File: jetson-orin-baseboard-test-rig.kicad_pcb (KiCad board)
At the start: 2 copper layers, 150 x 150 mm, 153 parts, among them J1 PinHeader_2x6_P2.54mm_Drill1.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, J2 PinHeader_2x6_P2.54mm_Drill1.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, J3 PinHeader_2x6_P2.54mm_Drill1.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, J4 PinHeader_2x6_P2.54mm_Drill1.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, J5 PinHeader_2x6_P2.54mm_Drill1.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, J6 PinHeader_2x6_P2.54mm_Drill1.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, J7 PinHeader_2x6_P2.54mm_Drill1.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, J9 Tag-Connect_TC2050-IDC-NL_2x5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

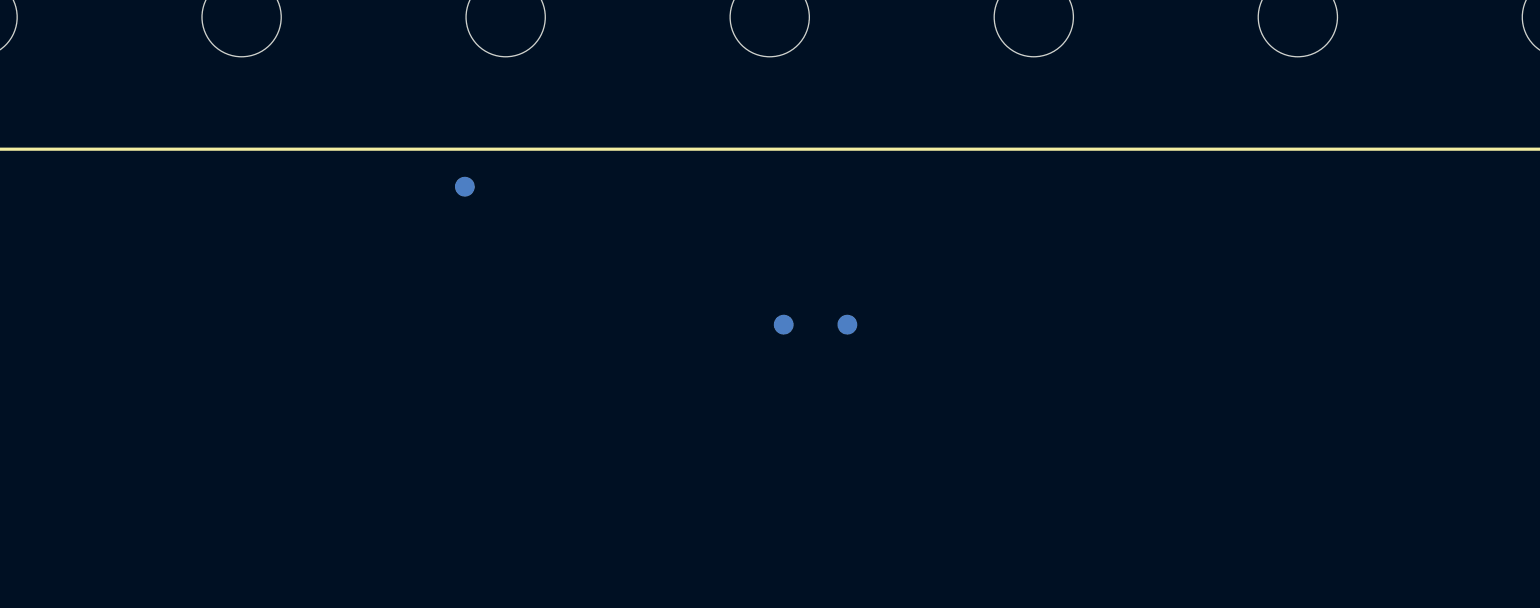
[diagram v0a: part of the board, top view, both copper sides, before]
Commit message: [#77400] Add spring probes (WiP)
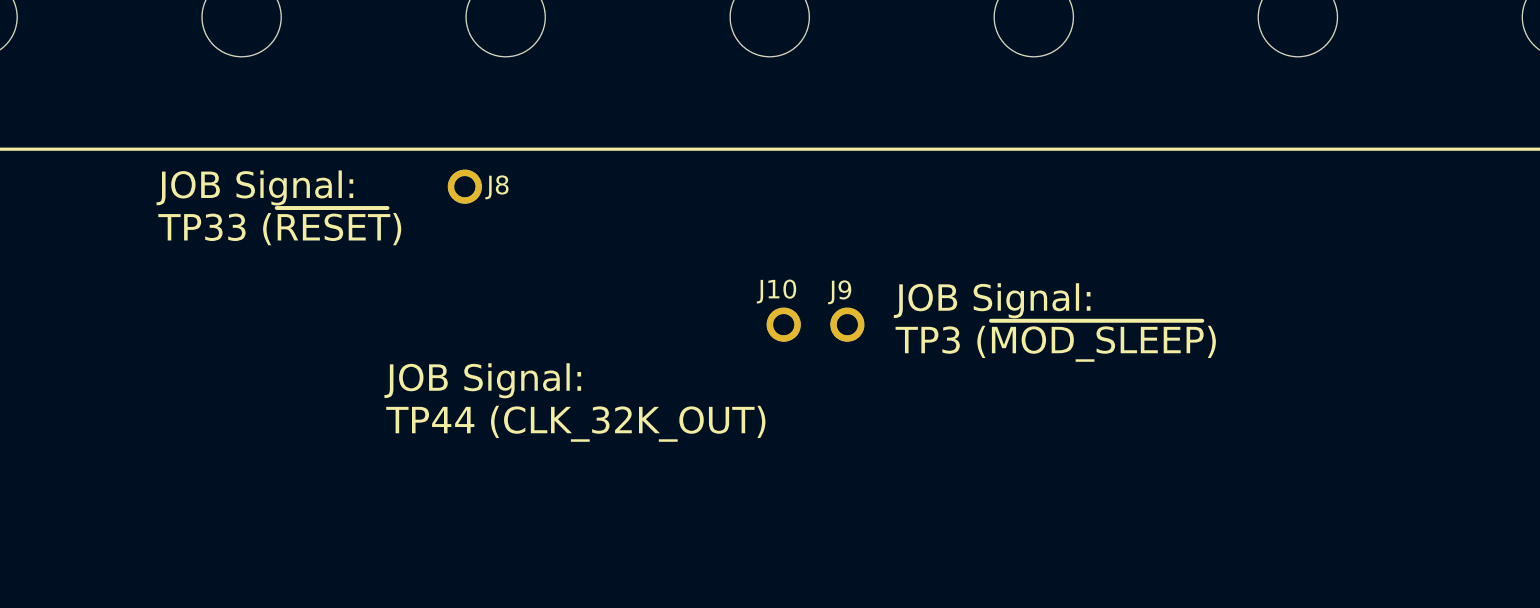
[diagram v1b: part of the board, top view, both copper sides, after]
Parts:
- removed TP3, TP33, TP44: TP_0.75mm_SMD, antmicro-footprints:TP_SMD_0.75mm
- added J10: Harwin_1x1_H17.75mm_Drill0.8mm_S13-503, antmicro-footprints:PogoPin_Harwin_1x1_H17.75mm_Drill0.8mm_S13-503, F.Cu at (210.5, 101.6)
- added J8: Harwin_1x1_H17.75mm_Drill0.8mm_S13-503, antmicro-footprints:PogoPin_Harwin_1x1_H17.75mm_Drill0.8mm_S13-503, F.Cu at (198.5, 96.4)
- added J9: Harwin_1x1_H17.75mm_Drill0.8mm_S13-503, antmicro-footprints:PogoPin_Harwin_1x1_H17.75mm_Drill0.8mm_S13-503, F.Cu at (212.9, 101.6)
- renumbered J9 to J999
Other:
- board text added: "JOB Signal: TP3 (~{MOD_SLEEP})"
- board text added: "JOB Signal: TP33 (~{RESET})"
- board text added: "JOB Signal: TP44 (CLK_32K_OUT)"

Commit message: [#77400] Finalize schematic
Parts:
- removed J999: Tag-Connect_TC2050-IDC-NL_2x5_P1.27mm, antmicro-footprints:Tag-Connect_TC2050-IDC-NL_2x5_P1.27mm
- removed TP1, TP13, TP14, TP17, TP22, TP23, TP29, TP30, TP31, TP32, TP52, TP53, TP54, TP55: TP_0.75mm_SMD, antmicro-footprints:TP_SMD_0.75mm
- added D1: LED_G_0603_KP-1608CGCK, antmicro-footprints:LED_0603_1608Metric_G, F.Cu at (298.6, 192.4)
- added D2: LED_G_0603_KP-1608CGCK, antmicro-footprints:LED_0603_1608Metric_G, F.Cu at (296.0, 192.4)
- added J11: Harwin_1x1_H17.75mm_Drill0.8mm_S13-503, antmicro-footprints:PogoPin_Harwin_1x1_H17.75mm_Drill0.8mm_S13-503, F.Cu at (199.0, 123.2)
- added J12: Harwin_1x1_H17.75mm_Drill0.8mm_S13-503, antmicro-footprints:PogoPin_Harwin_1x1_H17.75mm_Drill0.8mm_S13-503, F.Cu at (221.8, 128.6)
- added J13: Harwin_1x1_H17.75mm_Drill0.8mm_S13-503, antmicro-footprints:PogoPin_Harwin_1x1_H17.75mm_Drill0.8mm_S13-503, F.Cu at (243.3, 141.7)
- added J14: Harwin_1x1_H17.75mm_Drill0.8mm_S13-503, antmicro-footprints:PogoPin_Harwin_1x1_H17.75mm_Drill0.8mm_S13-503, F.Cu at (247.2, 130.3)
- added J15: Harwin_1x1_H17.75mm_Drill0.8mm_S13-503, antmicro-footprints:PogoPin_Harwin_1x1_H17.75mm_Drill0.8mm_S13-503, F.Cu at (214.9, 141.1)
- added J16: Harwin_1x1_H17.75mm_Drill0.8mm_S13-503, antmicro-footprints:PogoPin_Harwin_1x1_H17.75mm_Drill0.8mm_S13-503, F.Cu at (203.4, 141.8)
- added J17: Harwin_1x1_H17.75mm_Drill0.8mm_S13-503, antmicro-footprints:PogoPin_Harwin_1x1_H17.75mm_Drill0.8mm_S13-503, F.Cu at (203.4, 143.3)
- added J18: Harwin_1x1_H17.75mm_Drill0.8mm_S13-503, antmicro-footprints:PogoPin_Harwin_1x1_H17.75mm_Drill0.8mm_S13-503, F.Cu at (203.4, 144.8)
- added J19: Harwin_1x1_H17.75mm_Drill0.8mm_S13-503, antmicro-footprints:PogoPin_Harwin_1x1_H17.75mm_Drill0.8mm_S13-503, F.Cu at (203.4, 146.3)
- added J20: Harwin_1x1_H17.75mm_Drill0.8mm_S13-503, antmicro-footprints:PogoPin_Harwin_1x1_H17.75mm_Drill0.8mm_S13-503, F.Cu at (203.4, 147.8)
- added J21: Harwin_1x1_H17.75mm_Drill0.8mm_S13-503, antmicro-footprints:PogoPin_Harwin_1x1_H17.75mm_Drill0.8mm_S13-503, F.Cu at (203.4, 149.3)
- added J22: Harwin_1x1_H17.75mm_Drill0.8mm_S13-503, antmicro-footprints:PogoPin_Harwin_1x1_H17.75mm_Drill0.8mm_S13-503, F.Cu at (203.4, 150.8)
- added J23: Harwin_1x1_H17.75mm_Drill0.8mm_S13-503, antmicro-footprints:PogoPin_Harwin_1x1_H17.75mm_Drill0.8mm_S13-503, F.Cu at (203.4, 152.3)
- added J24: Harwin_1x1_H17.75mm_Drill0.8mm_S13-503, antmicro-footprints:PogoPin_Harwin_1x1_H17.75mm_Drill0.8mm_S13-503, F.Cu at (203.4, 153.8)
- added J25: Harwin_1x1_H17.75mm_Drill0.8mm_S13-503, antmicro-footprints:PogoPin_Harwin_1x1_H17.75mm_Drill0.8mm_S13-503, F.Cu at (221.8, 152.0)
- added J26: Harwin_1x1_H17.75mm_Drill0.8mm_S13-503, antmicro-footprints:PogoPin_Harwin_1x1_H17.75mm_Drill0.8mm_S13-503, F.Cu at (220.3, 152.2)
- added J27: Harwin_1x1_H17.75mm_Drill0.8mm_S13-503, antmicro-footprints:PogoPin_Harwin_1x1_H17.75mm_Drill0.8mm_S13-503, F.Cu at (217.9, 152.1)
- added J28: Harwin_1x1_H17.75mm_Drill0.8mm_S13-503, antmicro-footprints:PogoPin_Harwin_1x1_H17.75mm_Drill0.8mm_S13-503, F.Cu at (216.6, 150.9)
- added J29: Harwin_1x1_H17.75mm_Drill0.8mm_S13-503, antmicro-footprints:PogoPin_Harwin_1x1_H17.75mm_Drill0.8mm_S13-503, F.Cu at (219.2, 150.9)
- added J30: Harwin_1x1_H17.75mm_Drill0.8mm_S13-503, antmicro-footprints:PogoPin_Harwin_1x1_H17.75mm_Drill0.8mm_S13-503, F.Cu at (216.8, 120.1)
- added Q1: BSS84, antmicro-footprints:SOT-23-3, F.Cu at (246.2, 111.7)
- added R1: R_330R_0402, antmicro-footprints:R_0402_1005Metric, F.Cu at (298.6, 190.0)
- added R10: R_0R_0402, antmicro-footprints:R_0402_1005Metric, F.Cu at (239.6, 112.5)
- added R11: R_0R_0402, antmicro-footprints:R_0402_1005Metric, F.Cu at (239.6, 114.5)
- added R12: R_0R_0402, antmicro-footprints:R_0402_1005Metric, F.Cu at (239.6, 116.5)
- added R13: R_3k9_0402, antmicro-footprints:R_0402_1005Metric, F.Cu at (239.6, 118.5)
- added R14: R_68k_0402, antmicro-footprints:R_0402_1005Metric, F.Cu at (239.6, 120.5)
- added R15: R_68k_0402, antmicro-footprints:R_0402_1005Metric, F.Cu at (242.5, 110.6)
- added R16: R_68k_0402, antmicro-footprints:R_0402_1005Metric, F.Cu at (242.5, 112.5)
- added R17: R_68k_0402, antmicro-footprints:R_0402_1005Metric, F.Cu at (242.5, 114.5)
- added R18: R_0R_0402, antmicro-footprints:R_0402_1005Metric, F.Cu at (242.5, 116.5)
- added R19: R_10k_0402, antmicro-footprints:R_0402_1005Metric, F.Cu at (242.5, 118.5)
- added R2: R_3k9_0402, antmicro-footprints:R_0402_1005Metric, F.Cu at (296.0, 190.0)
- added R3: R_0R_0402, antmicro-footprints:R_0402_1005Metric, F.Cu at (236.7, 110.6)
- added R4: R_10k_0402, antmicro-footprints:R_0402_1005Metric, F.Cu at (236.7, 112.5)
- added R5: R_0R_0402, antmicro-footprints:R_0402_1005Metric, F.Cu at (236.7, 114.5)
- added R6: R_0R_0402, antmicro-footprints:R_0402_1005Metric, F.Cu at (236.7, 116.5)
- added R7: R_0R_0402, antmicro-footprints:R_0402_1005Metric, F.Cu at (236.7, 118.5)
- added R8: R_0R_0402, antmicro-footprints:R_0402_1005Metric, F.Cu at (236.7, 120.5)
- added R9: R_0R_0402, antmicro-footprints:R_0402_1005Metric, F.Cu at (239.6, 110.6)
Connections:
- J8 pad 1: /GPIO_00 -> Net-(J8-Pad1)
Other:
- board text added: "JOB Signal: SP7-Pin1 (GND)"
- board text added: "JOB Signal: TP13 (U6-Pin30)"
- board text added: "JOB Signal: TP17 (USBC0_VBUS)- TP1 (USBC3_VBUS)- TP29 (USBC1_VBUS)- TP14 (VCC)- TP53 (+5V)- TP54 (+3V3)- TP52 (3V3_STDB)- TP55 (+1V8)- TP23 (GND)-"
- board text added: "JOB Signal: TP22 (HDMI_HPD)"
- board text added: "JOB Signal: TP30 (USBC_HPD)"
- board text added: "JOB Signal: TP31 (USBC1_DIR)"
- board text added: "JOB Signal: TP32 (USBC1_FAULT_N)"
- board text removed: "+1V8"
- board text removed: "+3V3"
- board text removed: "+5V"
- board text removed: "3V3 STDB"
- board text removed: "EEPROM SPI"
- board text removed: "GND"
- board text removed: "VBUS0"
- board text removed: "VBUS1"
- board text removed: "VBUS3"
- board text removed: "VCC"

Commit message: [#77400] Finish routing
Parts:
- added REF**29: MP_NPTH_Drill3mm, antmicro-footprints:MP_NPTH_Drill3mm, F.Cu at (220.0, 110.0)
- added REF**29: MP_NPTH_Drill3mm, antmicro-footprints:MP_NPTH_Drill3mm, F.Cu at (170.0, 110.0)
- added REF**30: MP_NPTH_Drill3mm, antmicro-footprints:MP_NPTH_Drill3mm, F.Cu at (230.0, 110.0)
- added REF**30: MP_NPTH_Drill3mm, antmicro-footprints:MP_NPTH_Drill3mm, F.Cu at (180.0, 100.0)
- added REF**30: MP_NPTH_Drill3mm, antmicro-footprints:MP_NPTH_Drill3mm, F.Cu at (180.0, 110.0)
- added REF**31: MP_NPTH_Drill3mm, antmicro-footprints:MP_NPTH_Drill3mm, F.Cu at (190.0, 110.0)
- added REF**31: MP_NPTH_Drill3mm, antmicro-footprints:MP_NPTH_Drill3mm, F.Cu at (240.0, 110.0)
- added REF**32: MP_NPTH_Drill3mm, antmicro-footprints:MP_NPTH_Drill3mm, F.Cu at (170.0, 140.0)
- added REF**32: MP_NPTH_Drill3mm, antmicro-footprints:MP_NPTH_Drill3mm, F.Cu at (280.0, 120.0)
- added REF**32: MP_NPTH_Drill3mm, antmicro-footprints:MP_NPTH_Drill3mm, F.Cu at (190.0, 130.0)
- added REF**32: MP_NPTH_Drill3mm, antmicro-footprints:MP_NPTH_Drill3mm, F.Cu at (240.0, 120.0)
- added REF**32: MP_NPTH_Drill3mm, antmicro-footprints:MP_NPTH_Drill3mm, F.Cu at (190.0, 120.0)
- added REF**32: MP_NPTH_Drill3mm, antmicro-footprints:MP_NPTH_Drill3mm, F.Cu at (200.0, 130.0)
- added REF**32: MP_NPTH_Drill3mm, antmicro-footprints:MP_NPTH_Drill3mm, F.Cu at (250.0, 110.0)
- added REF**32: MP_NPTH_Drill3mm, antmicro-footprints:MP_NPTH_Drill3mm, F.Cu at (270.0, 110.0)
- added REF**32: MP_NPTH_Drill3mm, antmicro-footprints:MP_NPTH_Drill3mm, F.Cu at (170.0, 130.0)
- added REF**32: MP_NPTH_Drill3mm, antmicro-footprints:MP_NPTH_Drill3mm, F.Cu at (200.0, 110.0)
- added REF**32: MP_NPTH_Drill3mm, antmicro-footprints:MP_NPTH_Drill3mm, F.Cu at (260.0, 120.0)
- added REF**32: MP_NPTH_Drill3mm, antmicro-footprints:MP_NPTH_Drill3mm, F.Cu at (270.0, 130.0)
- added REF**32: MP_NPTH_Drill3mm, antmicro-footprints:MP_NPTH_Drill3mm, F.Cu at (170.0, 120.0)
- added REF**33: MP_NPTH_Drill3mm, antmicro-footprints:MP_NPTH_Drill3mm, F.Cu at (260.0, 110.0)
- added REF**33: MP_NPTH_Drill3mm, antmicro-footprints:MP_NPTH_Drill3mm, F.Cu at (240.0, 150.0)
- added REF**33: MP_NPTH_Drill3mm, antmicro-footprints:MP_NPTH_Drill3mm, F.Cu at (270.0, 140.0)
- added REF**33: MP_NPTH_Drill3mm, antmicro-footprints:MP_NPTH_Drill3mm, F.Cu at (230.0, 140.0)
- added REF**33: MP_NPTH_Drill3mm, antmicro-footprints:MP_NPTH_Drill3mm, F.Cu at (260.0, 150.0)
- added REF**33: MP_NPTH_Drill3mm, antmicro-footprints:MP_NPTH_Drill3mm, F.Cu at (180.0, 130.0)
- added REF**33: MP_NPTH_Drill3mm, antmicro-footprints:MP_NPTH_Drill3mm, F.Cu at (280.0, 140.0)
- added REF**33: MP_NPTH_Drill3mm, antmicro-footprints:MP_NPTH_Drill3mm, F.Cu at (210.0, 150.0)
- added REF**33: MP_NPTH_Drill3mm, antmicro-footprints:MP_NPTH_Drill3mm, F.Cu at (250.0, 150.0)
- added REF**33: MP_NPTH_Drill3mm, antmicro-footprints:MP_NPTH_Drill3mm, F.Cu at (230.0, 120.0)
- added REF**33: MP_NPTH_Drill3mm, antmicro-footprints:MP_NPTH_Drill3mm, F.Cu at (180.0, 120.0)
- added REF**33: MP_NPTH_Drill3mm, antmicro-footprints:MP_NPTH_Drill3mm, F.Cu at (270.0, 150.0)
- added REF**33: MP_NPTH_Drill3mm, antmicro-footprints:MP_NPTH_Drill3mm, F.Cu at (280.0, 130.0)
- added REF**33: MP_NPTH_Drill3mm, antmicro-footprints:MP_NPTH_Drill3mm, F.Cu at (280.0, 110.0)
- added REF**33: MP_NPTH_Drill3mm, antmicro-footprints:MP_NPTH_Drill3mm, F.Cu at (230.0, 150.0)
- added REF**33: MP_NPTH_Drill3mm, antmicro-footprints:MP_NPTH_Drill3mm, F.Cu at (260.0, 140.0)
- added REF**33: MP_NPTH_Drill3mm, antmicro-footprints:MP_NPTH_Drill3mm, F.Cu at (180.0, 140.0)
- added REF**33: MP_NPTH_Drill3mm, antmicro-footprints:MP_NPTH_Drill3mm, F.Cu at (210.0, 120.0)
- added REF**33: MP_NPTH_Drill3mm, antmicro-footprints:MP_NPTH_Drill3mm, F.Cu at (250.0, 120.0)
- added REF**33: MP_NPTH_Drill3mm, antmicro-footprints:MP_NPTH_Drill3mm, F.Cu at (210.0, 110.0)
- added REF**33: MP_NPTH_Drill3mm, antmicro-footprints:MP_NPTH_Drill3mm, F.Cu at (240.0, 130.0)
- added REF**33: MP_NPTH_Drill3mm, antmicro-footprints:MP_NPTH_Drill3mm, F.Cu at (270.0, 120.0)
- added REF**33: MP_NPTH_Drill3mm, antmicro-footprints:MP_NPTH_Drill3mm, F.Cu at (210.0, 130.0)
- added REF**34: MP_NPTH_Drill3mm, antmicro-footprints:MP_NPTH_Drill3mm, F.Cu at (220.0, 100.0)
- added REF**35: MP_NPTH_Drill3mm, antmicro-footprints:MP_NPTH_Drill3mm, F.Cu at (230.0, 100.0)
- added REF**36: MP_NPTH_Drill3mm, antmicro-footprints:MP_NPTH_Drill3mm, F.Cu at (240.0, 100.0)
- added REF**37: MP_NPTH_Drill3mm, antmicro-footprints:MP_NPTH_Drill3mm, F.Cu at (250.0, 100.0)
- added REF**38: MP_NPTH_Drill3mm, antmicro-footprints:MP_NPTH_Drill3mm, F.Cu at (260.0, 100.0)
- added REF**39: MP_NPTH_Drill3mm, antmicro-footprints:MP_NPTH_Drill3mm, F.Cu at (270.0, 100.0)
- moved R15 112.5 mm to (161.3, 188.4), turned to 90 degrees
- moved R16 112.1 mm to (160.0, 188.4), turned to 90 degrees
- moved R17 111.7 mm to (158.7, 188.4), turned to 90 degrees
- moved R10 106.4 mm to (165.1, 188.4), turned to 90 degrees
- moved R11 104.0 mm to (166.3, 188.4), turned to 90 degrees
- moved R13 103.1 mm to (163.8, 188.4), turned to -90 degrees
- moved R14 102.7 mm to (162.5, 188.4), turned to 90 degrees
- moved R12 101.7 mm to (167.6, 188.4), turned to 90 degrees
- moved R6 87.7 mm to (286.4, 188.8), turned to 90 degrees
- moved R5 85.3 mm to (278.7, 188.8), turned to 90 degrees
- moved R7 83.2 mm to (281.3, 188.8), turned to 90 degrees
- moved R8 83.0 mm to (283.8, 188.8), turned to 90 degrees
- moved R3 79.9 mm to (218.7, 188.4), turned to 90 degrees
- moved R9 79.9 mm to (229.5, 189.8)
- moved Q1 77.8 mm to (228.9, 187.6), turned to 180 degrees
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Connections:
- J19 pad 1: Net-(J19-Pad1) -> VCC
- R10 pad 1: /ADC_A_IN5 -> /ADC_A_IN6
- R11 pad 1: /ADC_A_IN6 -> /ADC_A_IN3
- R13 pad 2: /ADC_A_IN4 -> /ADC_A_IN2
- R14 pad 1: /ADC_A_IN3 -> /ADC_A_IN5
- R14 pad 2: Net-(J19-Pad1) -> VCC
- R15 pad 1: /ADC_A_IN2 -> /ADC_A_IN1
- R16 pad 1: /ADC_A_IN1 -> /ADC_A_IN4
- R9 pad 1: /GPIO_01 -> /GPIO_02
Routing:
- net VCC: track 0.00 -> 216.3 mm, vias 0 -> 1
- net +3V3: track 0.00 -> 202.9 mm
- net Net-(J28-Pad1): track 0.00 -> 116.9 mm, vias 0 -> 1
- net Net-(J27-Pad1): track 0.00 -> 104.1 mm, vias 0 -> 1
- net Net-(J8-Pad1): track 0.00 -> 100.0 mm, vias 0 -> 1
- net Net-(J29-Pad1): track 0.00 -> 97.0 mm, vias 0 -> 1
- net Net-(J26-Pad1): track 0.00 -> 91.2 mm, vias 0 -> 1
- net Net-(J16-Pad1): track 0.00 -> 78.9 mm, vias 0 -> 1
- net Net-(J17-Pad1): track 0.00 -> 76.2 mm, vias 0 -> 1
- net Net-(J20-Pad1): track 0.00 -> 74.2 mm, vias 0 -> 1
- net Net-(J18-Pad1): track 0.00 -> 73.8 mm, vias 0 -> 1
- net Net-(J30-Pad1): track 0.00 -> 73.1 mm, vias 0 -> 1
- net Net-(J21-Pad1): track 0.00 -> 71.5 mm, vias 0 -> 1
- net Net-(J22-Pad1): track 0.00 -> 69.0 mm, vias 0 -> 1
- net Net-(J23-Pad1): track 0.00 -> 66.5 mm, vias 0 -> 1
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- added copper zone on F.Cu, net GND
- removed copper zone on B.Cu, net GND
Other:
- board text added: "+3V3"
- board text added: "MISO SCLK MOSI CS0 EEPROM_PWR"
- board text added: "VCC"
